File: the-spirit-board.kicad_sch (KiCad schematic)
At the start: 12 parts, among them IC1 ESP32-C6-WROOM-1-N8, IC2 AP2112K-3.3TRG1

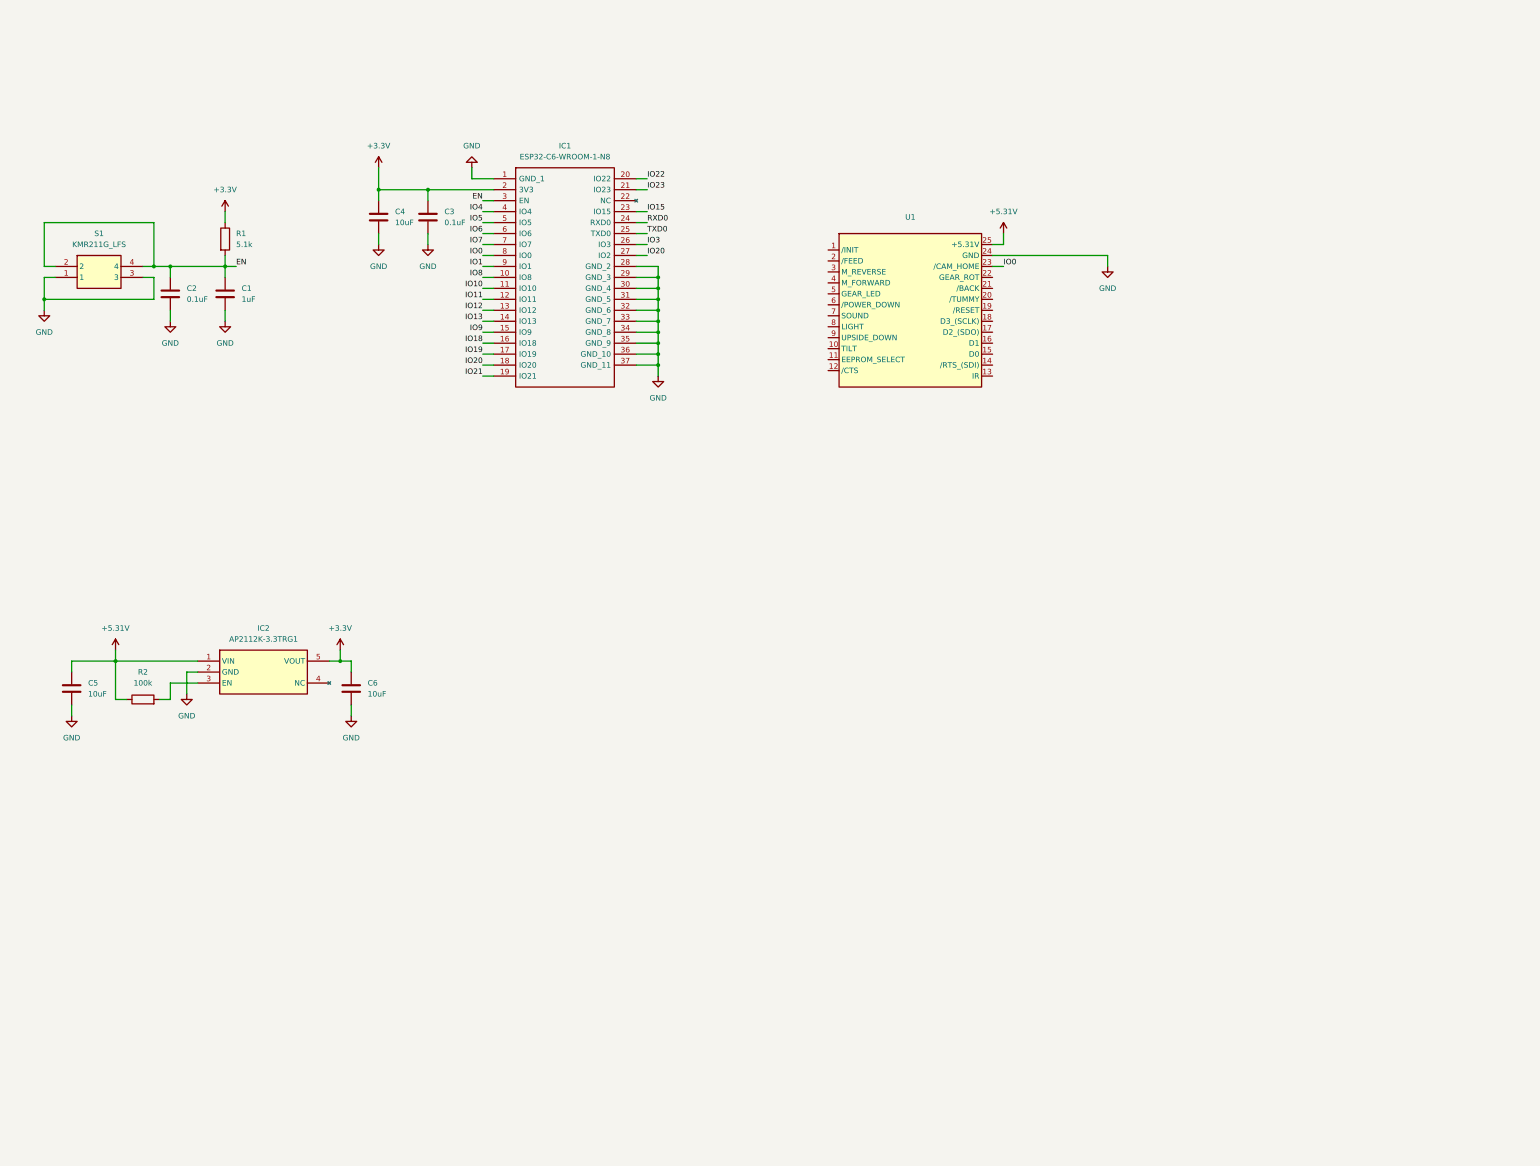
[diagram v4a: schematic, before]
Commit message: Completed connection between the Furby and the ESP32-C6
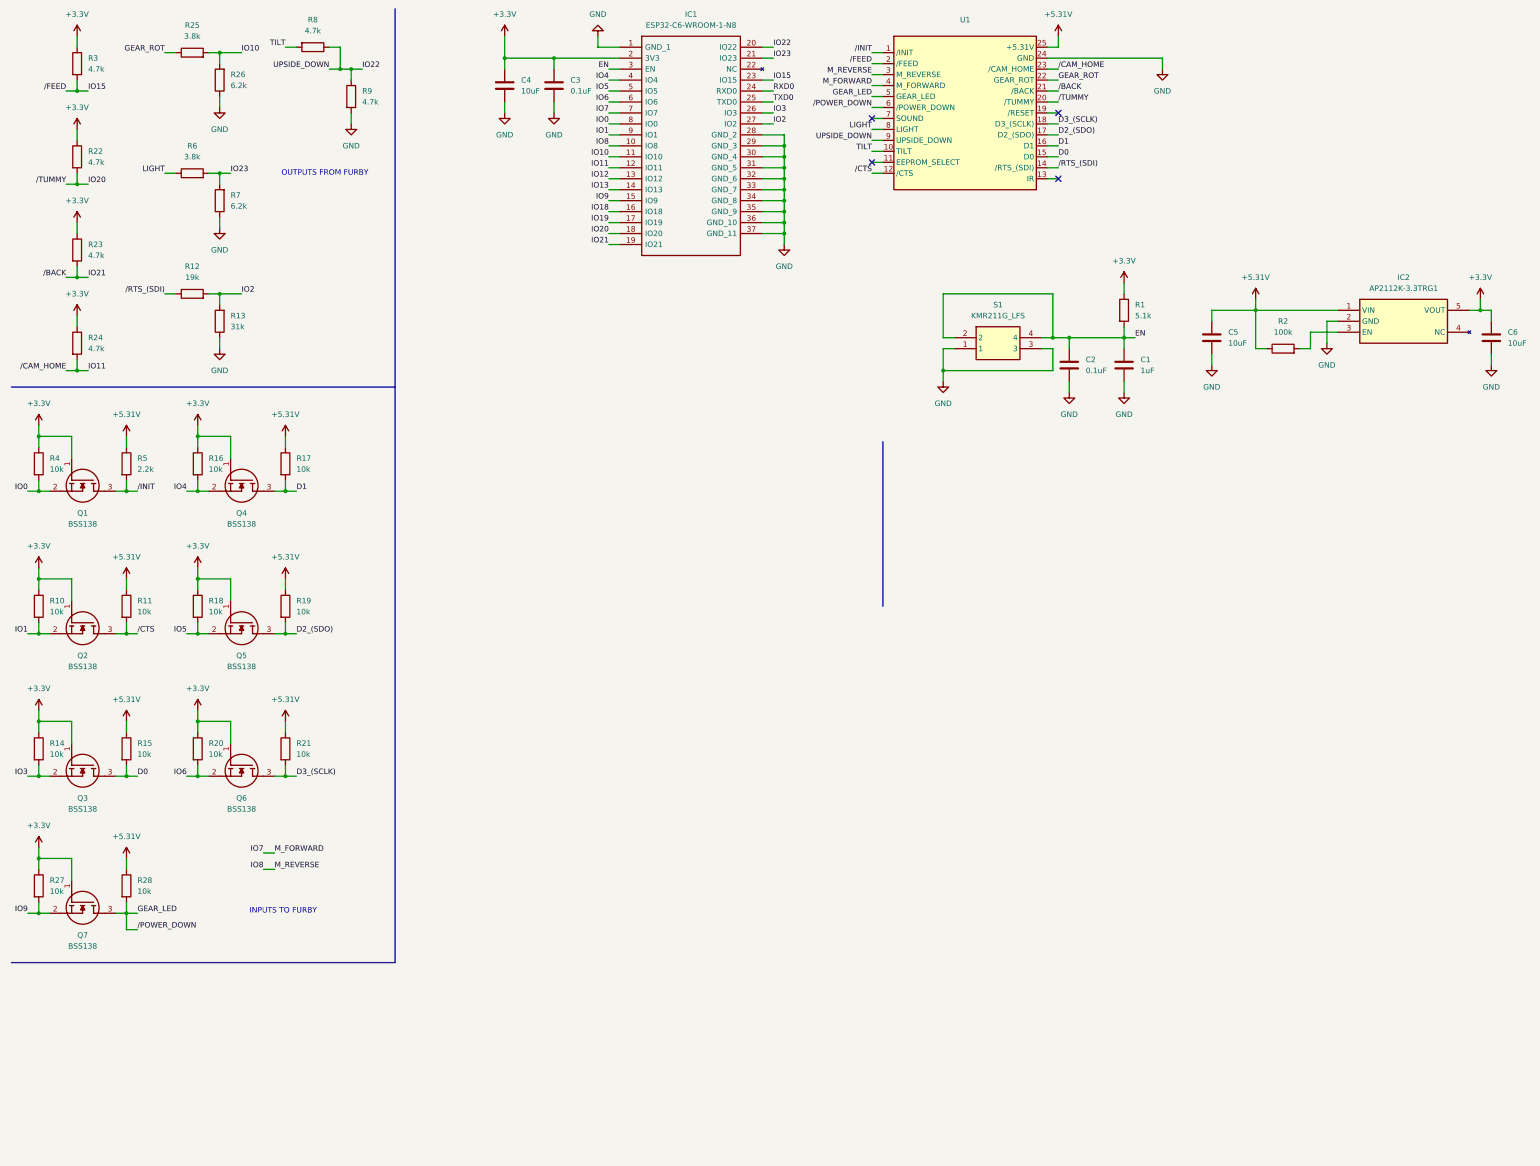
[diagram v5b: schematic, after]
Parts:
- added Q1, Q2, Q3, Q4, Q5, Q6, Q7: BSS138, SOT95P240X120-3N, symbol TheSPIRITBoard:BSS138
- added R10, R11, R14, R15, R16, R17, R18, R19, R20, R21, R27, R28, R4: 10k, Resistor_SMD:R_0603_1608Metric, symbol Device:R
- added R12: 19k, Resistor_SMD:R_0603_1608Metric, symbol Device:R
- added R13: 31k, Resistor_SMD:R_0603_1608Metric, symbol Device:R
- added R22, R23, R24, R3, R8, R9: 4.7k, Resistor_SMD:R_0603_1608Metric, symbol Device:R
- added R25, R6: 3.8k, Resistor_SMD:R_0603_1608Metric, symbol Device:R
- added R26, R7: 6.2k, Resistor_SMD:R_0603_1608Metric, symbol Device:R
- added R5: 2.2k, Resistor_SMD:R_0603_1608Metric, symbol Device:R
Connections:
- net +3.3V: now also Q1.1 (G), Q2.1 (G), Q3.1 (G), Q4.1 (G), Q5.1 (G), Q6.1 (G), Q7.1 (G), R10.1, R14.1, R16.1, R18.1, R20.1, R22.1, R23.1, R24.1, R27.1, R3.1, R4.1
- net +5.31V: now also R11.1, R15.1, R17.1, R19.1, R21.1, R28.1, R5.1
- net GND: now also R13.1, R26.1, R7.1, R9.2
- net IO0: now also Q1.2 (S), R4.2; no longer U1.23 (/CAM_HOME)
- net IO1: now also Q2.2 (S), R10.2
- net IO10: now also R25.2, R26.2
- net IO11: now also U1.23 (/CAM_HOME), R24.2
- net IO15: now also U1.2 (/FEED), R3.2
- net IO20: now also U1.20 (/TUMMY), R22.2; no longer IC1.27 (IO2)
- net IO21: now also U1.21 (/BACK), R23.2
- net IO22: now also U1.9 (UPSIDE_DOWN), R8.1, R9.1
- net IO23: now also R6.2, R7.2
- net IO3: now also Q3.2 (S), R14.2
- net IO4: now also Q4.2 (S), R16.2
- net IO5: now also Q5.2 (S), R18.2
- net IO6: now also Q6.2 (S), R20.2
- net IO7: now also U1.4 (M_FORWARD)
- net IO8: now also U1.3 (M_REVERSE)
- net IO9: now also Q7.2 (S), R27.2
- net /INIT: now reaches U1.1 (/INIT)
- net /INIT: now also Q1.3 (D), R5.2
- net TILT: now reaches U1.10 (TILT)
- net TILT: now also R8.2
- net /CTS: now reaches U1.12 (/CTS)
- net /CTS: now also Q2.3 (D), R11.2
- net /RTS_(SDI): now reaches U1.14 (/RTS_(SDI))
- net /RTS_(SDI): now also R12.1
- net D0: now reaches U1.15 (D0)
- net D0: now also Q3.3 (D), R15.2
- net D1: now reaches U1.16 (D1)
- net D1: now also Q4.3 (D), R17.2
- net D2_(SDO): now reaches U1.17 (D2_(SDO))
- net D2_(SDO): now also Q5.3 (D), R19.2
- net D3_(SCLK): now reaches U1.18 (D3_(SCLK))
- net D3_(SCLK): now also Q6.3 (D), R21.2
- net GEAR_ROT: now reaches U1.22 (GEAR_ROT)
- net GEAR_ROT: now also R25.1
- net GEAR_LED: now reaches U1.5 (GEAR_LED)
- net GEAR_LED: now also U1.6 (/POWER_DOWN), Q7.3 (D), R28.2
- net LIGHT: now reaches U1.8 (LIGHT)
- net LIGHT: now also R6.1
- new net IO2: IC1.27 (IO2), R12.2, R13.2
- no-connect marks 0 -> 4
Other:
- note added: "INPUTS TO FURBY"
- note added: "OUTPUTS FROM FURBY"
- moved on the sheet: C1, C2, C3, C4, C5, C6, IC1, IC2, R1, R2, S1, U1

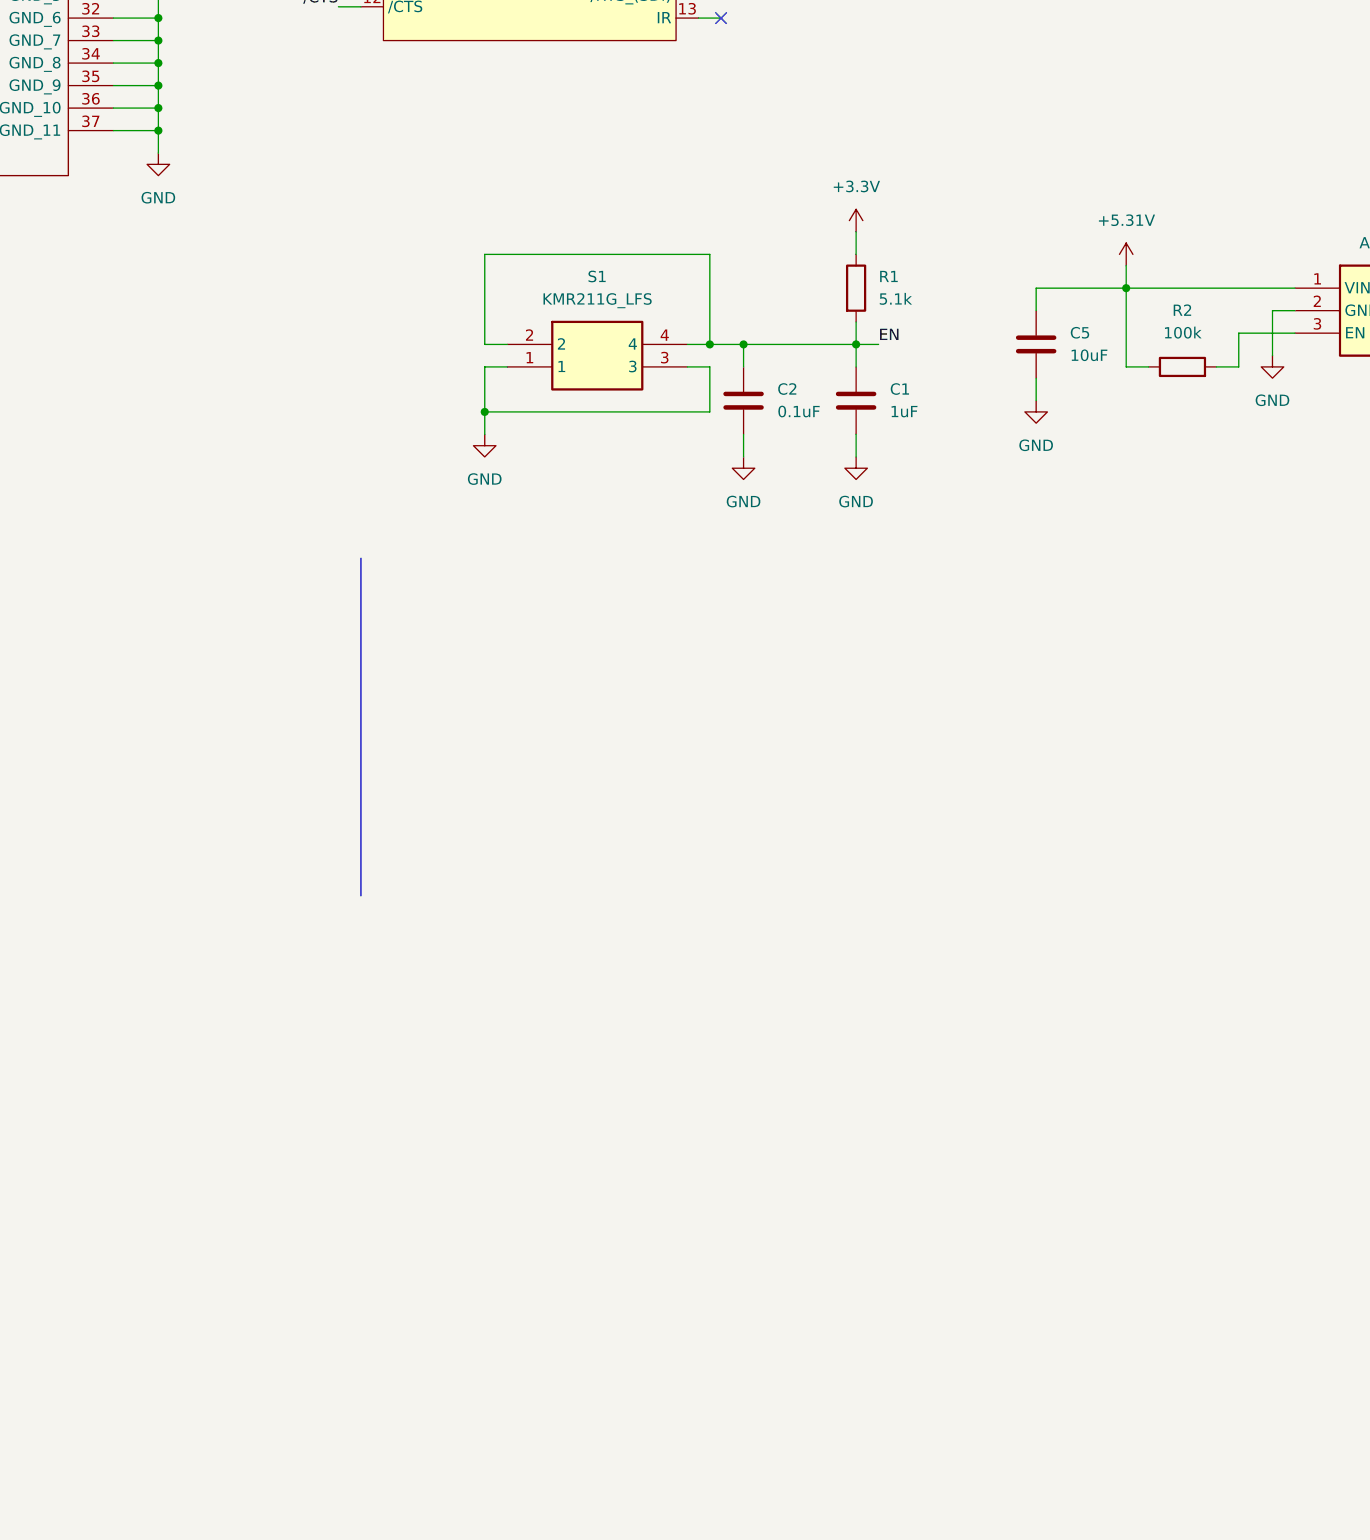
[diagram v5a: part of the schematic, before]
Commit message: Add USB-C connection
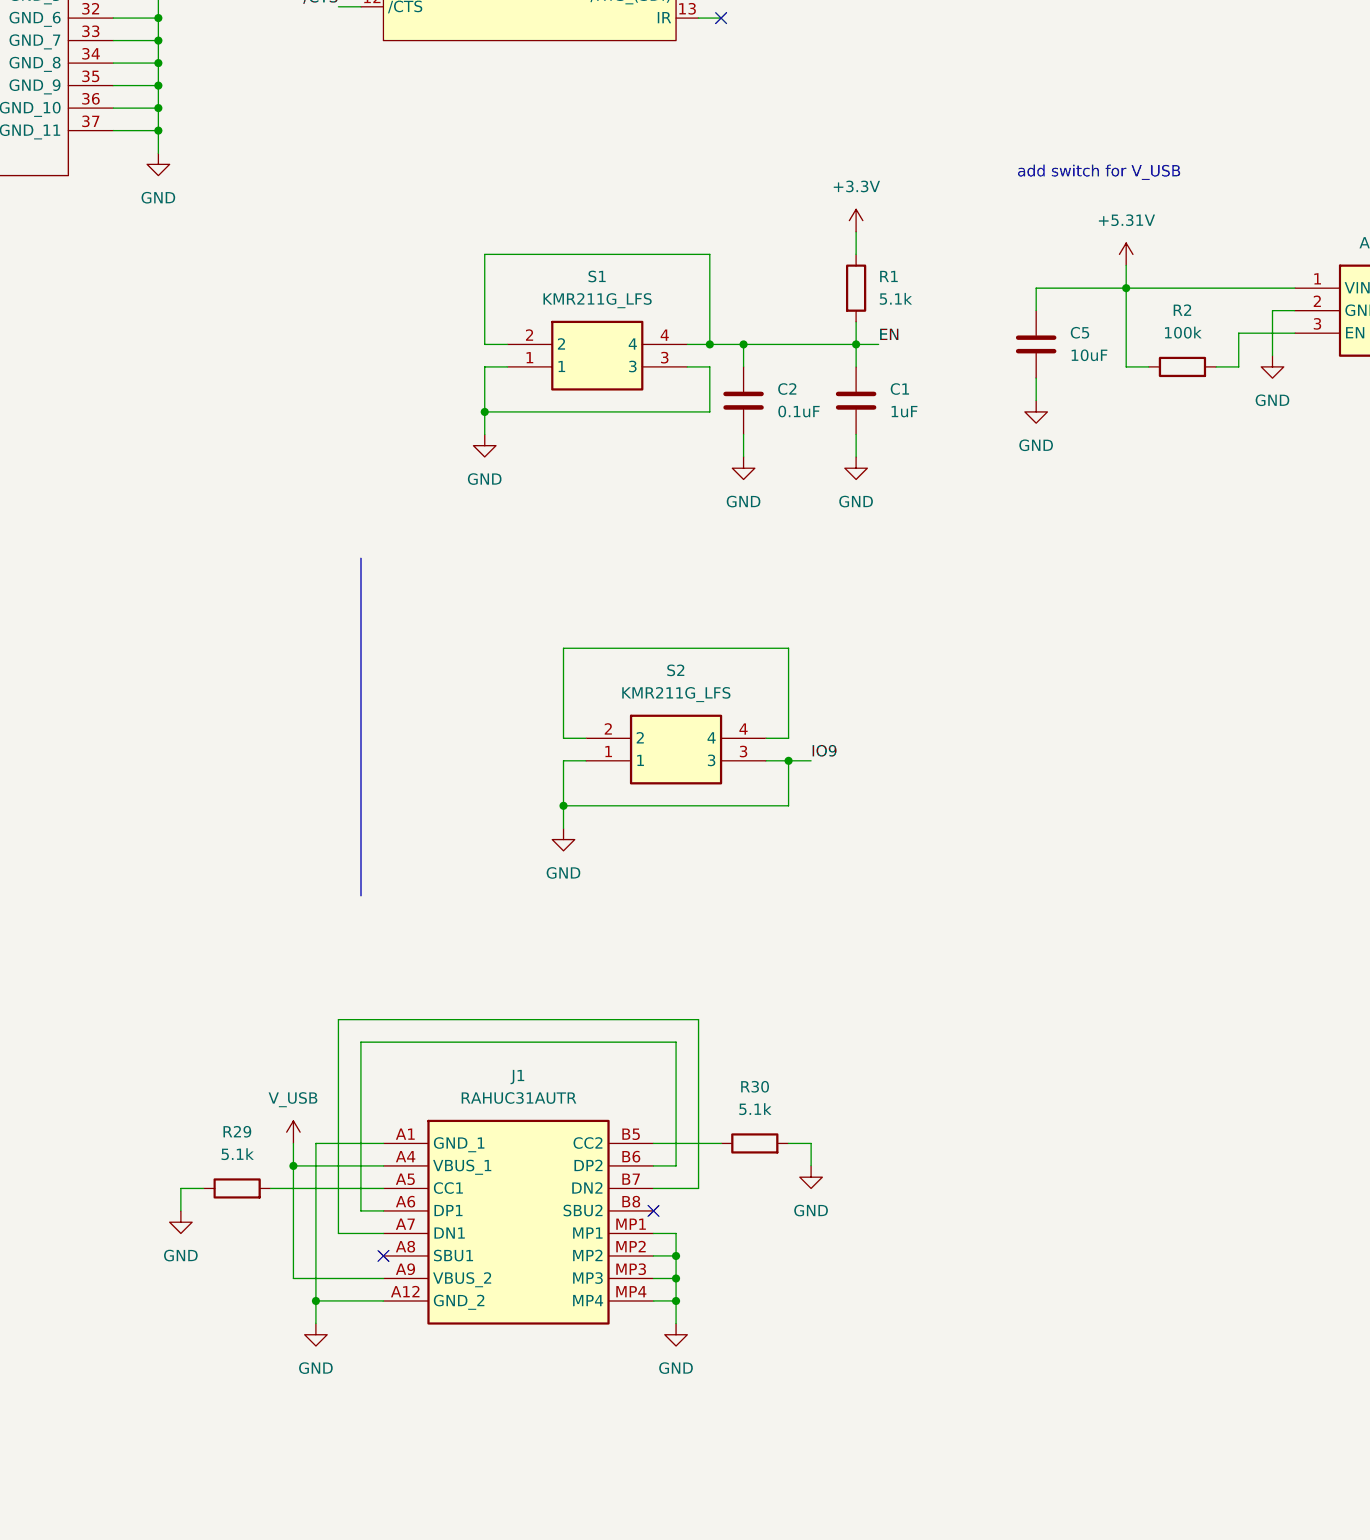
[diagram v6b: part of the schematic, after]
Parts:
- added J1: RAHUC31AUTR, RAHUC31AUTR, symbol TheSPIRITBoard:RAHUC31AUTR
- added R29, R30: 5.1k, Resistor_SMD:R_0603_1608Metric, symbol Device:R
- added S2: KMR211G_LFS, KMR_2, symbol TheSPIRITBoard:KMR211G_LFS
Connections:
- net IO9 is gone; now on net GND: IC1.15 (IO9), Q7.2 (S), R27.2
- net GND: now also J1.A1 (GND_1), J1.A12 (GND_2), J1.MP1, J1.MP2, J1.MP3, J1.MP4, R29.1, R30.2, S2.1, S2.3
- new net: J1.A5 (CC1), R29.2
- new net: J1.B5 (CC2), R30.1
- new net: J1.A6 (DP1), J1.B6 (DP2)
- new net: J1.A7 (DN1), J1.B7 (DN2)
- new net: S2.2, S2.4
- new net V_USB: J1.A4 (VBUS_1), J1.A9 (VBUS_2)
- no-connect marks 4 -> 6
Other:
- note added: "add switch for V_USB"
